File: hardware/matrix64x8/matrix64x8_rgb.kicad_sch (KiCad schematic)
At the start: 59 parts, among them J1 Screw_Terminal_01x08, J3 RESET DISABLE (Remove to prog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, Q0 FQP47P06, U0 74HCT238, U1 ULN2803A*, U11 THVD1439, U12 74HCT238, U13 74HCT238, U14 ULN2803A*, U15 ULN2803A*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

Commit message: protocol notes
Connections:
- net at J1.3 (Pin_3), J?.8 (Pin_8): no longer C0.2, J3.1 (A)
- new net: C0.2, J3.1 (A)
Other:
- note added: "3.2.2"
- note added: "R_{4} R_{3} R_{2} R_{1} R_{0} 0 0 x x x Red plane 0 1 x x x Green plane 1 0 x x x Blue plane 1 1 x x x Display off x x 0 0 0 Row 0 (top) x x 0 0 1 Row 1 x x 0 1 0 Row 2 x x 0 1 1 Row 3 x x 1 0 0 Row 4 x x 1 0 1 Row 5 x x 1 1 0 Row 6 x x 1 1 1 Row 7 (bottom)"
- note removed: "3.2.1"
- note removed: "R_{4} R_{3} R_{2} R_{1} R_{0} 0 0 x x x Red plane 0 1 x x x Green plane 1 0 x x x Blue plane 1 1 x x x Display off"
- moved on the sheet: C0, J3
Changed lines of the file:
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@@
 	)
 	(junction
-		(at 177.8 234.95)
-		(diameter 0)
-		(color 0 0 0 0)
-	)
-	(junction
 		(at 88.9 184.15)
 		(diameter 0)
@@
 	(wire
 		(pts
-			(xy 177.8 234.95) (xy 255.27 234.95)
-		)
-		(stroke
-			(width 0)
-			(type default)
-		)
-	)
-	(wire
-		(pts
 			(xy 140.97 52.07) (xy 145.415 52.07)
 		)
@@
 	(wire
 		(pts
-			(xy 177.8 234.95) (xy 177.8 236.22)
+			(xy 177.8 220.472) (xy 177.8 221.742)
 		)
 		(stroke
@@
 	(wire
 		(pts
-			(xy 170.18 223.52) (xy 170.18 234.95)
+			(xy 170.18 223.52) (xy 170.18 239.014)
 		)
 		(stroke
@@
 	(wire
 		(pts
-			(xy 177.8 246.38) (xy 177.8 251.46)
+			(xy 177.8 231.902) (xy 177.8 234.188)
 		)
 		(stroke
@@
 	(wire
 		(pts
-			(xy 255.27 234.95) (xy 255.27 215.9)
+			(xy 255.27 239.014) (xy 255.27 215.9)
 		)
 		(stroke
@@
 	(wire
 		(pts
-			(xy 177.8 210.82) (xy 177.8 227.33)
+			(xy 177.8 210.82) (xy 177.8 212.852)
 		)
 		(stroke
@@
 	(wire
 		(pts
-			(xy 170.18 234.95) (xy 177.8 234.95)
+			(xy 170.18 239.014) (xy 255.27 239.014)
 		)
 		(stroke
@@
 		)
 	)
-	(text "R_{4} R_{3} R_{2} R_{1} R_{0}\n 0  0  x  x  x  Red plane\n 0  1  x  x  x  Green plane\n 1  0  x  x  x  Blue plane\n 1  1  x  x  x  Display off"
+	(text "R_{4} R_{3} R_{2} R_{1} R_{0}\n 0  0  x  x  x  Red plane\n 0  1  x  x  x  Green plane\n 1  0  x  x  x  Blue plane\n 1  1  x  x  x  Display off\n x  x  0  0  0  Row 0 (top)\n x  x  0  0  1  Row 1\n x  x  0  1  0  Row 2\n x  x  0  1  1  Row 3\n x  x  1  0  0  Row 4\n x  x  1  0  1  Row 5\n x  x  1  1  0  Row 6\n x  x  1  1  1  Row 7 (bottom)"
 		(exclude_from_sim no)
-		(at 26.035 168.275 0)
+		(at 23.114 189.23 0)
 		(effects
 			(font
@@
 		)
 	)
-	(text "3.2.1"
+	(text "3.2.2"
 		(exclude_from_sim no)
 		(at 405.13 263.525 0)
@@
 	(symbol
 		(lib_id "Jumper:Jumper_2_Bridged")
-		(at 177.8 241.3 270)
+		(at 177.8 226.822 270)
 		(unit 1)
 		(exclude_from_sim no)
@@
 		(on_board yes)
 		(dnp no)
-		(fields_autoplaced yes)
 		(property "Reference" "J3"
-			(at 180.34 240.0299 90)
+			(at 178.054 230.632 90)
 			(effects
 				(font
@@
 		)
 		(property "Value" "RESET DISABLE (Remove to program)"
-			(at 180.34 242.5699 90)
+			(at 178.054 232.664 90)
 			(effects
 				(font
@@
 		)
 		(property "Footprint" ""
-			(at 177.8 241.3 0)
+			(at 177.8 226.822 0)
 			(effects
 				(font
@@
 		)
 		(property "Datasheet" "~"
-			(at 177.8 241.3 0)
+			(at 177.8 226.822 0)
 			(effects
 				(font
@@
 		)
 		(property "Description" ""
-			(at 177.8 241.3 0)
+			(at 177.8 226.822 0)
 			(effects
 				(font
@@
 	(symbol
 		(lib_id "Device:C_Polarized_US")
-		(at 177.8 231.14 0)
+		(at 177.8 216.662 0)
 		(unit 1)
 		(exclude_from_sim no)
@@
 		(on_board yes)
 		(dnp no)
-		(fields_autoplaced yes)
 		(property "Reference" "C0"
-			(at 180.975 229.235 0)
+			(at 178.054 214.376 0)
 			(effects
 				(font
@@
 		)
 		(property "Value" "10µF"
-			(at 180.975 231.775 0)
+			(at 178.308 219.456 0)
 			(effects
 				(font
@@
 		)
 		(property "Footprint" ""
-			(at 177.8 231.14 0)
+			(at 177.8 216.662 0)
 			(effects
 				(font
@@
 		)
 		(property "Datasheet" "~"
-			(at 177.8 231.14 0)
+			(at 177.8 216.662 0)
 			(effects
 				(font
@@
 		)
 		(property "Description" ""
-			(at 177.8 231.14 0)
+			(at 177.8 216.662 0)
 			(effects
 				(font
@@
 	(symbol
 		(lib_id "power:GNDREF")
-		(at 177.8 251.46 0)
+		(at 177.8 234.188 0)
 		(unit 1)
 		(exclude_from_sim no)
@@
 		(fields_autoplaced yes)
 		(property "Reference" "#PWR01"
-			(at 177.8 257.81 0)
+			(at 177.8 240.538 0)
 			(effects
 				(font
@@
 		)
 		(property "Value" "GNDREF"
-			(at 177.8 255.905 0)
+			(at 177.8 238.633 0)
 			(effects
 				(font
@@
 		)
 		(property "Footprint" ""
-			(at 177.8 251.46 0)
+			(at 177.8 234.188 0)
 			(effects
 				(font
@@
 		)
 		(property "Datasheet" ""
-			(at 177.8 251.46 0)
+			(at 177.8 234.188 0)
 			(effects
 				(font
@@
 		)
 		(property "Description" ""
-			(at 177.8 251.46 0)
+			(at 177.8 234.188 0)
 			(effects
 				(font

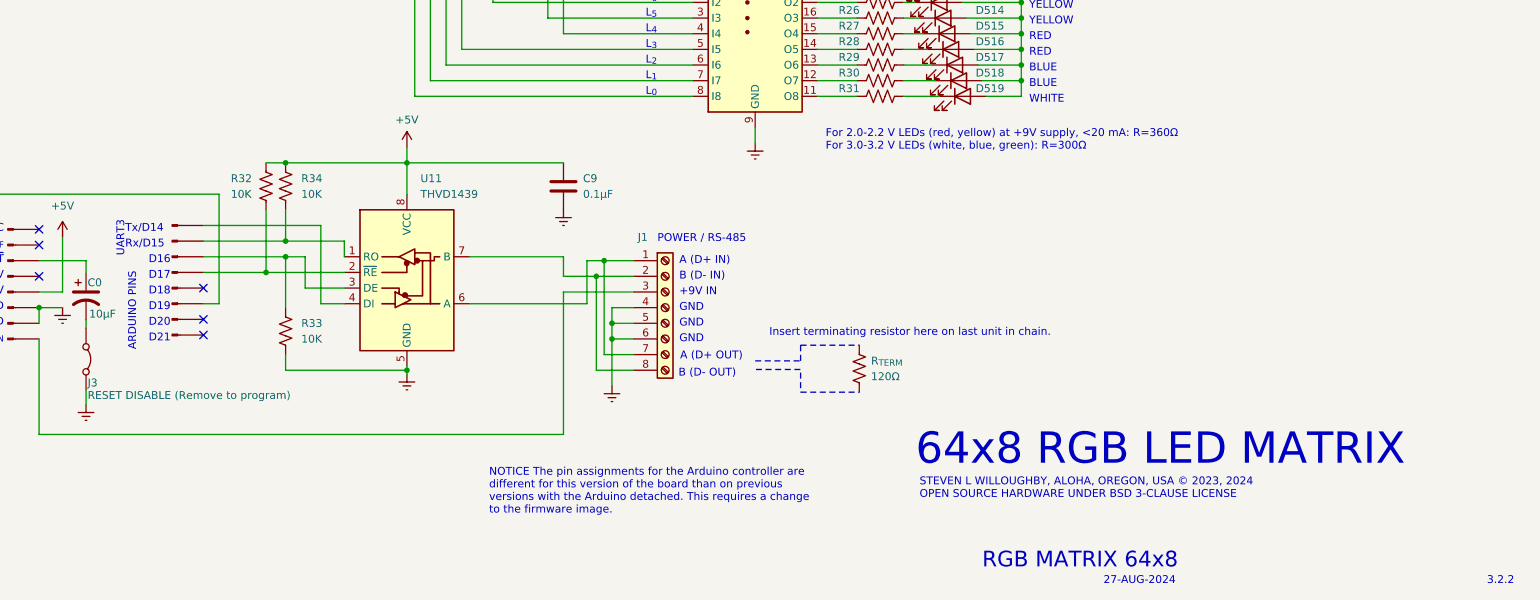
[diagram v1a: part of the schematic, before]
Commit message: corrected R34 placement on schematic to match what is actually on the PCB 3.2.2
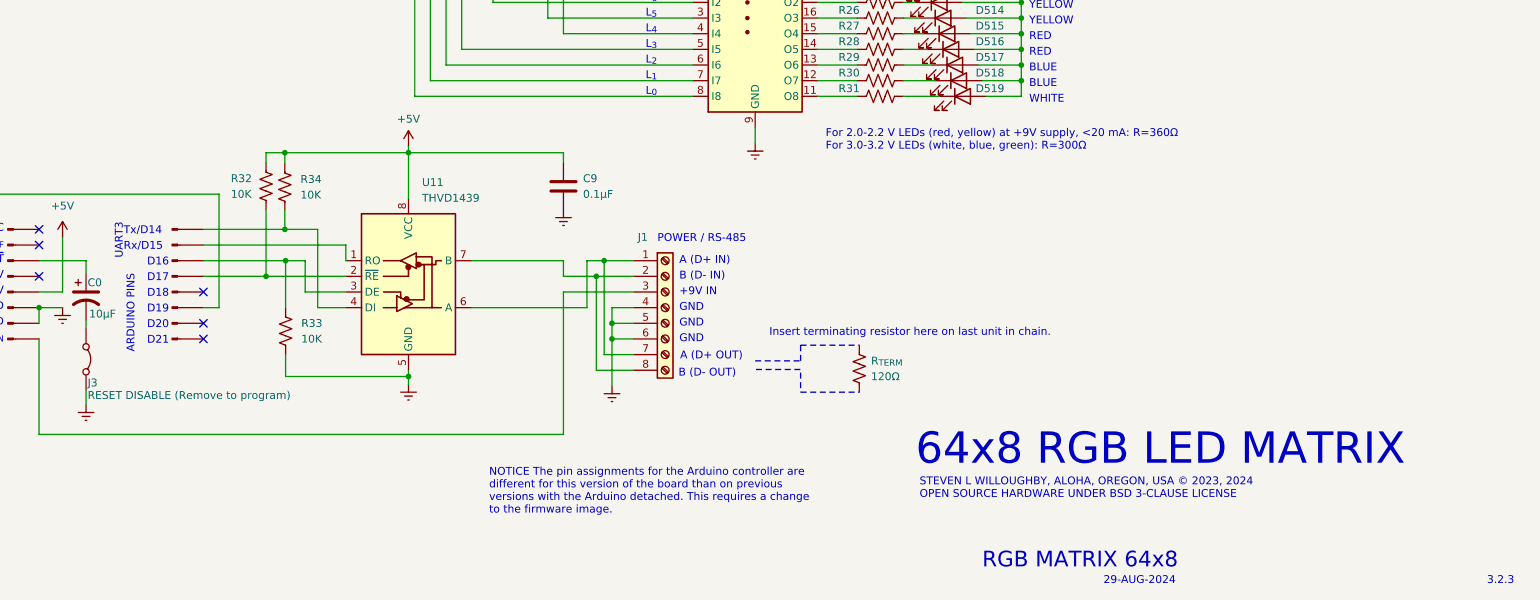
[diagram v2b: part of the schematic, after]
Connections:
- net at J?.2 (Pin_2), U11.1 (RO): no longer R34.2
- net at J?.1 (Pin_1), U11.4 (DI): now also R34.2
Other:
- note added: "29-AUG-2024"
- note added: "3.2.3"
- note removed: "27-AUG-2024"
- note removed: "3.2.2"
- moved on the sheet: U11

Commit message: wip
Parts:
- added J3: RESET, symbol Jumper:Jumper_2_Bridged
- added J4: EEPROM VOLTAGE, symbol Jumper:Jumper_3_Bridged12
- added J5: EEPROM, symbol Connector:Conn_01x04_Socket
- added R51: 1K, symbol Device:R_US
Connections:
- net +5V: now also J4.1 (A)
- net GNDREF: now also J1.7 (Pin_7), J3.2 (B), J5.1 (Pin_1); no longer J1.4 (Pin_4)
- net at J1.1 (Pin_1), U11.6 (A): now also J1.3 (Pin_3); no longer J1.7 (Pin_7)
- net at J1.2 (Pin_2), U11.7 (B): now also J1.4 (Pin_4); no longer J1.8 (Pin_8)
- net at C0.1, J?.3 (Pin_3): now also J3.1 (A), R51.2
- net +3.3V: now reaches J?.4 (Pin_4)
- net +3.3V: now also J4.3 (B), R51.1
- net at J?.8 (Pin_8): now also J1.8 (Pin_8); no longer J1.3 (Pin_3)
- net at J?.7 (Pin_7): now also J5.2 (Pin_2)
- net at J?.8 (Pin_8): now also J5.3 (Pin_3)
- new net: J4.2 (C), J5.4 (Pin_4)
- no-connect marks 21 -> 18
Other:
- note added: "16-SEP-2024"
- note added: "3.3.0"
- note added: "ARDUINO DUE ONLY"
- note added: "MEGA 2560 ONLY"
- note added: "SCL"
- note added: "SDA"
- note added: "Vcc"
- note removed: "29-AUG-2024"
- note removed: "3.2.3"
- note removed: "D20"
- note removed: "D21"
- moved on the sheet: C9, J1, R32, R33, R34, R_{TERM}, U11

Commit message: wip
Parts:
- removed J5: EEPROM, symbol Connector:Conn_01x04_Socket
- added R52, R53: 10K, symbol Device:R_US
- added U16: AT24C256, Package_SO:SOIC-8_3.9x4.9mm_P1.27mm, symbol Memory_EEPROM:AT24CS01-SSHM
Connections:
- net GNDREF: now also U16.1 (A0), U16.2 (A1), U16.3 (A2), U16.4 (GND), U16.7 (WP)
- net at J?.7 (Pin_7): now also R53.2, U16.5 (SDA)
- net at J?.8 (Pin_8): now also R52.2, U16.6 (SCL)
- net at J4.2 (C): now also R52.1, R53.1, U16.8 (VCC)
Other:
- note removed: "Vcc"
- moved on the sheet: J4

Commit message: 001
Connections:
- net +9V: now also J1.8 (Pin_8), J?.8 (Pin_8)
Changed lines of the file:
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@@
 	)
 	(junction
+		(at 266.7 226.06)
+		(diameter 0)
+		(color 0 0 0 0)
+	)
+	(junction
 		(at 277.495 132.08)
 		(diameter 0)
@@
 	(wire
 		(pts
-			(xy 271.526 226.06) (xy 271.526 239.014)
+			(xy 266.7 226.06) (xy 266.7 239.014)
 		)
 		(stroke
@@
 	(wire
 		(pts
+			(xy 266.7 226.06) (xy 282.956 226.06)
+		)
+		(stroke
+			(width 0)
+			(type default)
+		)
+	)
+	(wire
+		(pts
 			(xy 89.535 139.7) (xy 89.535 114.3)
 		)
@@
 	(wire
 		(pts
+			(xy 266.7 220.98) (xy 266.7 226.06)
+		)
+		(stroke
+			(width 0)
+			(type default)
+		)
+	)
+	(wire
+		(pts
 			(xy 282.956 210.82) (xy 277.368 210.82)
 		)
@@
 	(wire
 		(pts
-			(xy 282.956 226.06) (xy 271.526 226.06)
-		)
-		(stroke
-			(width 0)
-			(type default)
-		)
-	)
-	(wire
-		(pts
 			(xy 91.44 228.6) (xy 64.77 228.6)
 		)
@@
 	(wire
 		(pts
-			(xy 162.56 239.014) (xy 271.526 239.014)
+			(xy 162.56 239.014) (xy 266.7 239.014)
 		)
 		(stroke
@@
 					(unit 1)
 				)
+			)
+		)
+	)
+	(symbol
+		(lib_id "power:+5V")
+		(at 266.7 220.98 0)
+		(unit 1)
+		(exclude_from_sim no)
+		(in_bom yes)
+		(on_board yes)
+		(dnp no)
+		(fields_autoplaced yes)
+		(property "Reference" "#PWR026"
+			(at 266.7 224.79 0)
+			(effects
+				(font
+					(size 1.27 1.27)
+				)
+				(hide yes)
+			)
+		)
+		(property "Value" "+9V"
+			(at 266.7 215.9 0)
+			(effects
+				(font
+					(size 1.27 1.27)
+				)
+			)
+		)
+		(property "Footprint" ""
+			(at 266.7 220.98 0)
+			(effects
+				(font
+					(size 1.27 1.27)
+				)
+				(hide yes)
+			)
+		)
+		(property "Datasheet" ""
+			(at 266.7 220.98 0)
+			(effects
+				(font
+					(size 1.27 1.27)
+				)
+				(hide yes)
+			)
+		)
+		(property "Description" ""
+			(at 266.7 220.98 0)
+			(effects
+				(font
+					(size 1.27 1.27)
+				)
+				(hide yes)
+			)
+		)
+		(pin "1"
+		)
+		(instances
+			(project "matrix64x8_rgb"
+				(path "/68206880-187a-441b-ad1d-285a8d6fa444"
+					(reference "#PWR026")
+					(unit 1)
+				)
